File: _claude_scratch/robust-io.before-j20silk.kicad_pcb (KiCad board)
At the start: 4 copper layers, 160 x 100 mm, 304 parts, among them J1 AVR-ISP-6, J10 Screw_Terminal_01x06, J14 Screw_Terminal_01x04, J15 Screw_Terminal_01x04, J16 Screw_Terminal_01x06, J18 Screw_Terminal_01x06, J19 Screw_Terminal_01x06, J20 UART, J3 Screw_Terminal_01x06, J4 Screw_Terminal_01x04, J5 Screw_Terminal_01x06, J6 Screw_Terminal_01x06, J9 Screw_Terminal_01x06, Q3 2N7002, Q4 2N7002, SW1 CHS-01TB, SW2 B3U-1000P, U1 DRV8876, U10 BTS7008, U11 BTS7008, U14 DRV8876, U2 ATmega1284P-A, U3 MCP2515, U4 TPS5604, U5 TPS5604, U6 MCP2562-E-MF, U7 MC33978, U8 BTS7008, U9 BTS7008, Y1 16MHz, Y2 12MHz

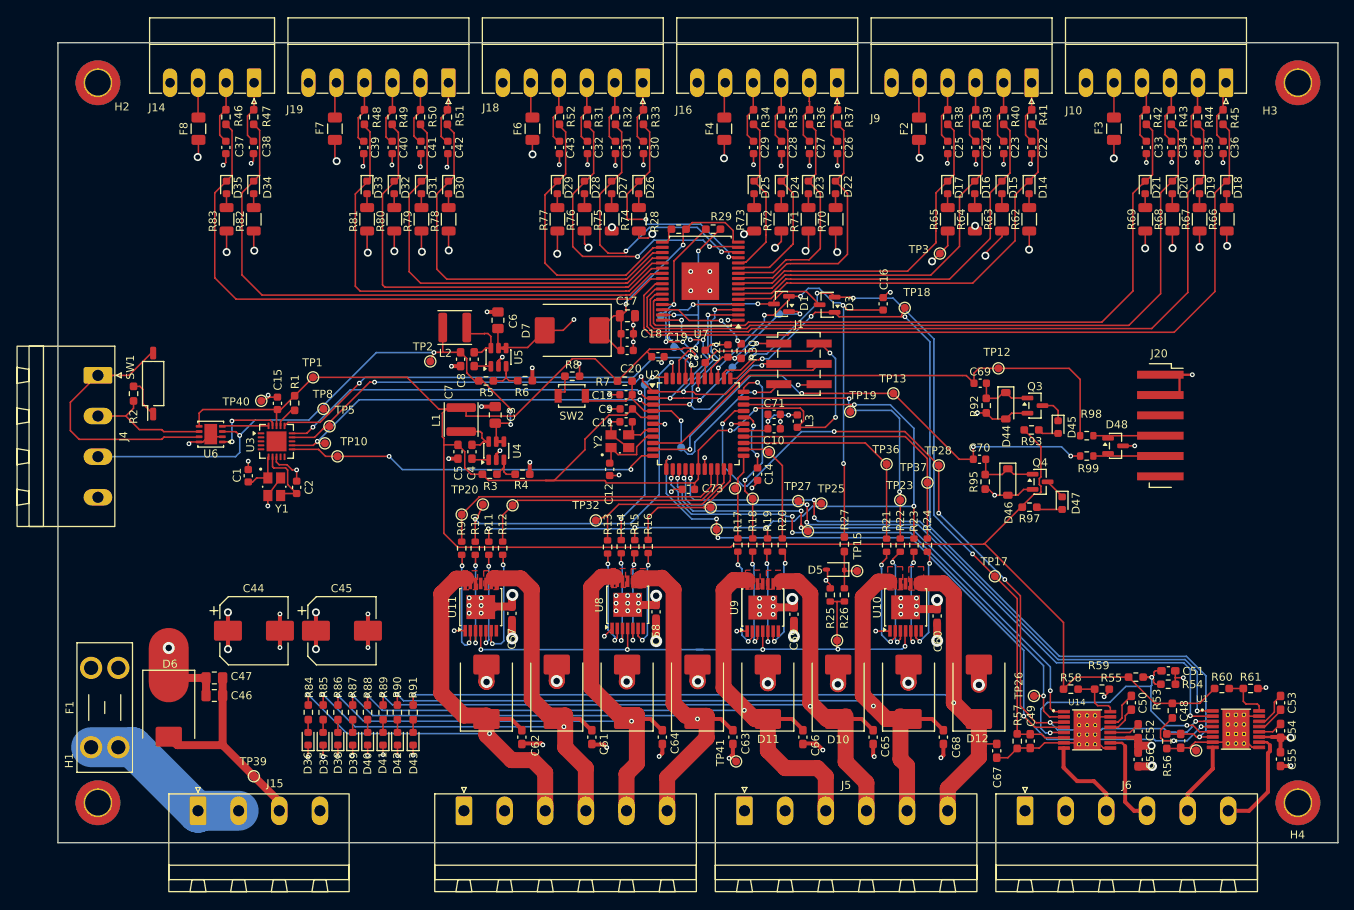
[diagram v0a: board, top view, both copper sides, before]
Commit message: Rev A: release to fab (JLCPCB, 5 PCB / 2 assembled)
Board
- Outline set to exactly 160 x 100 mm; plane zones resized to match
- UART brought out on J20 (1x6 SMD, FTDI pinout) with series
  resistors R98/R99 and TVS D48
- J1 and J20 changed to SMD headers (C52016780, C41417363)
- L1/L2 moved to Sunlord SWPA4030S footprints; regulator tracks rerouted
- 41 test points added (35 top, 6 bottom), including SPI access
- Crystal case pins (Y1/Y2 pads 2, 4) tied to GND
- SW2 changed to 2-pin push button symbol
- R84-R91 changed from 2.2k to 10k to cut dissipation at 24 V
- Thermal vias in U1/U14 enlarged to 0.3 mm drill; 27 +24V vias added
  under U8-U11; solid plane connections on high-current pins
- Input/output rows and edge connectors aligned
- /inputs/_SG4 track and via moved clear of R74 pad 1

Schematic
- ERC cleared: no-connects, PWR_FLAGs, pin types, off-grid items
- Symbols moved to project library robust-io
- Test point symbols added on processor and power sheets

Rules
- Custom DRC rule for U7 pad-to-pad clearance (0.15 mm)
- Minimum through hole 0.2 mm; silk-to-edge check ignored

Fab outputs (fab/)
- make_gerbers.sh: Gerbers, drill and position export via kicad-cli
- JLC BOM with LCSC part numbers on all 50 SMD lines
- JLC placement file with per-part rotation offsets
  (cpl_rotation_offsets.json), verified in JLC placement preview
- Through-hole BOM and test point list

DRC: 4 library-mismatch warnings (J20, U1, U14, U7), 0 errors
ERC: clean
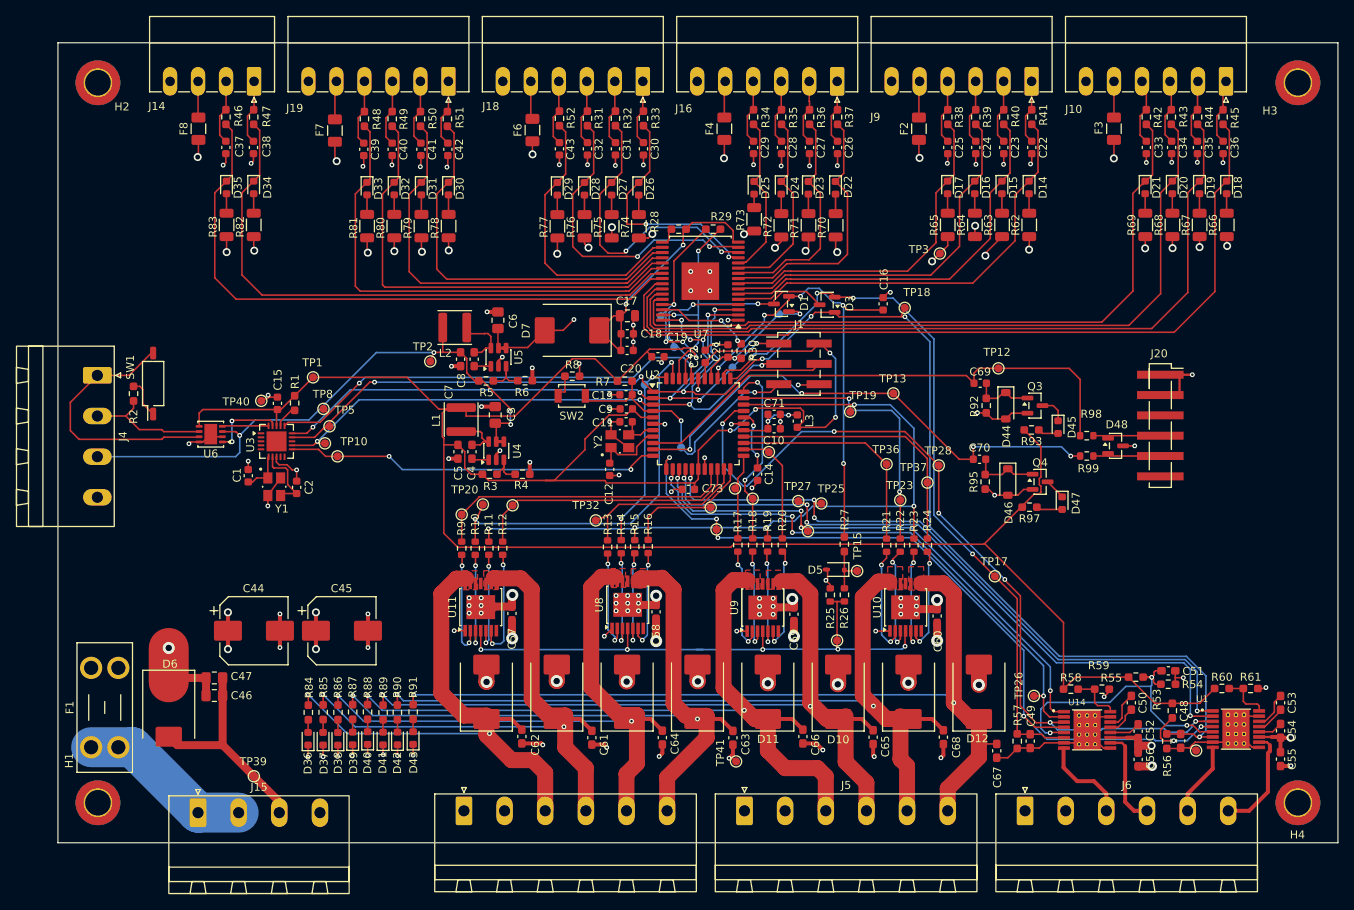
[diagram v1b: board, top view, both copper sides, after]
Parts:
- moved R74 0.87 mm to (102.6, 52.9)
- moved R75 0.87 mm to (99.2, 52.9)
- moved R76 0.87 mm to (95.8, 52.9)
- moved R77 0.87 mm to (92.4, 52.9)
- moved R78 0.85 mm to (78.8, 52.9)
- moved R79 0.85 mm to (75.4, 52.9)
- moved R80 0.85 mm to (72.0, 52.9)
- moved R81 0.85 mm to (68.6, 52.9)
- moved R70 0.75 mm to (127.2, 52.8)
- moved R71 0.75 mm to (123.8, 52.8)
- moved R72 0.75 mm to (120.4, 52.8)
- moved R62 0.70 mm to (151.4, 52.8)
- moved R63 0.70 mm to (148.0, 52.8)
- moved R64 0.70 mm to (144.6, 52.8)
- moved R65 0.70 mm to (141.2, 52.8)
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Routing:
- net +24V: track 131.6 -> 118.2 mm
- net GND: track 258.0 -> 256.5 mm
- net Net-(D29-A): track 1.74 -> 2.44 mm
- net Net-(D33-A): track 1.74 -> 2.44 mm
- net Net-(D32-A): track 1.74 -> 2.44 mm
- net Net-(D30-A): track 1.74 -> 2.44 mm
- net Net-(D28-A): track 1.74 -> 2.44 mm
- net Net-(D26-A): track 1.74 -> 2.44 mm
- net Net-(D23-A): track 1.74 -> 2.44 mm
- net Net-(D35-A): track 1.74 -> 2.44 mm
- net Net-(D34-A): track 1.74 -> 2.44 mm
- net Net-(D24-A): track 1.74 -> 2.44 mm
- net Net-(D22-A): track 1.74 -> 2.44 mm
- net Net-(D21-A): track 1.74 -> 2.44 mm
- net Net-(D20-A): track 1.74 -> 2.44 mm
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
